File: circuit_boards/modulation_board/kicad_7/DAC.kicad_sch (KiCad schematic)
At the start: 58 parts, among them U10 TL072, U503 LM4040C-2.5, U8 DAC8162xDGSx, U803 MCP6002-xSN, U9 DAC128S085CIMT

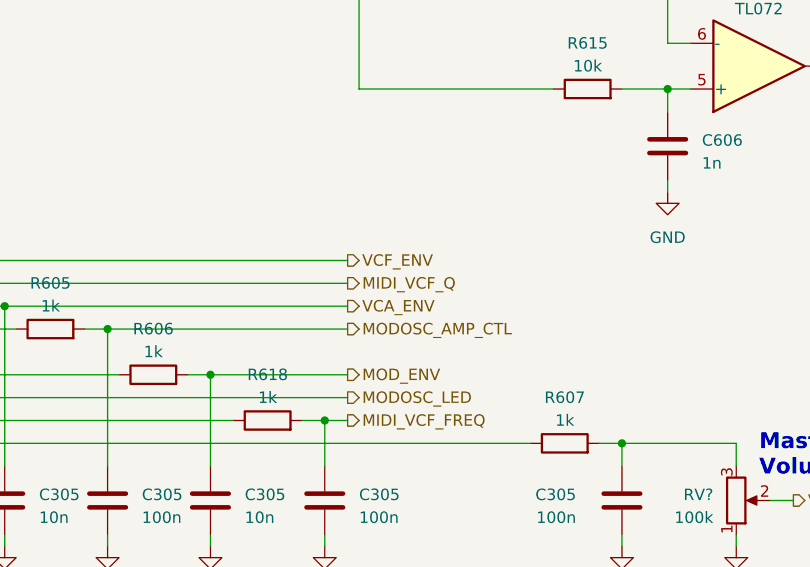
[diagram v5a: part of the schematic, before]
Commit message: Swap mixed up vcf/vca env signals
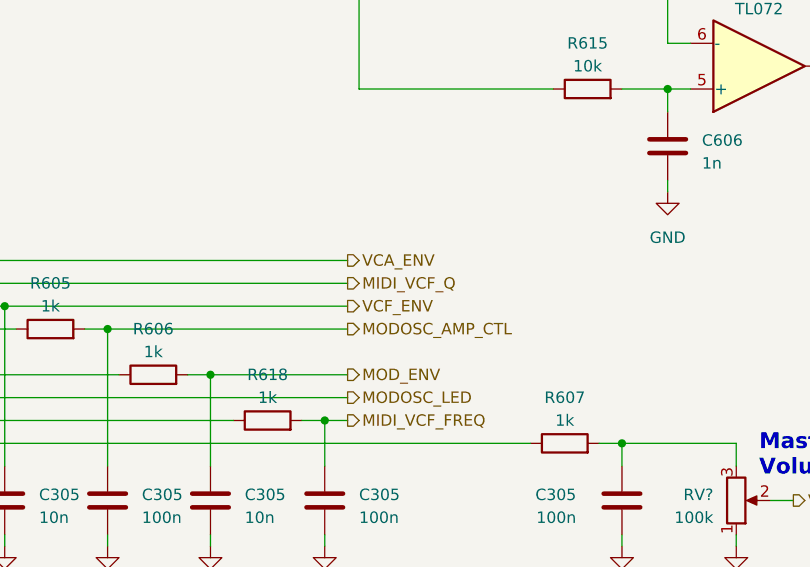
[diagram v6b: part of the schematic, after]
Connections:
- net VCA_ENV: now also C305.1, R602.2; no longer C305.1, R604.2
- net VCF_ENV: now also C305.1, R604.2; no longer C305.1, R602.2
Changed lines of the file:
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@@
     (effects (font (size 1.27 1.27)) (justify left))
   )
-  (hierarchical_label "VCA_ENV" (shape output) (at 170.18 111.76 0) (fields_autoplaced)
+  (hierarchical_label "VCA_ENV" (shape output) (at 170.18 106.68 0) (fields_autoplaced)
     (effects (font (size 1.27 1.27)) (justify left))
   )
@@
     (effects (font (size 1.27 1.27)) (justify left))
   )
-  (hierarchical_label "VCF_ENV" (shape output) (at 170.18 106.68 0) (fields_autoplaced)
+  (hierarchical_label "VCF_ENV" (shape output) (at 170.18 111.76 0) (fields_autoplaced)
     (effects (font (size 1.27 1.27)) (justify left))
   )
